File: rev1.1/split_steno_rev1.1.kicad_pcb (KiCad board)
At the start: 2 copper layers, 0 parts

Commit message: laid out switch footprints
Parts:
- added C1: 100, Capacitors_THT:CP_Radial_D5.0mm_P2.00mm, B.Cu at (170.2, 31.9)
- added D1: D, Keebio-Parts:Diode-dual, B.Cu at (65.5, 95.2)
- added D10: D, Keebio-Parts:Diode-dual, B.Cu at (141.7, 114.3)
- added D11: D, Keebio-Parts:Diode-dual, B.Cu at (65.5, 133.3)
- added D12: D, Keebio-Parts:Diode-dual, B.Cu at (86.9, 133.3)
- added D13: D, Keebio-Parts:Diode-dual, B.Cu at (103.6, 133.3)
- added D14: D, Keebio-Parts:Diode-dual, B.Cu at (106.0, 133.3)
- added D15: D, Keebio-Parts:Diode-dual, B.Cu at (141.7, 133.3)
- added D16: D, Keebio-Parts:Diode-dual, B.Cu at (96.4, 147.6)
- added D17: D, Keebio-Parts:Diode-dual, B.Cu at (111.9, 144.1)
- added D18: D, Keebio-Parts:Diode-dual, B.Cu at (136.9, 144.1)
- added D2: D, Keebio-Parts:Diode-dual, B.Cu at (86.9, 95.2)
- added D3: D, Keebio-Parts:Diode-dual, B.Cu at (103.6, 95.2)
- added D4: D, Keebio-Parts:Diode-dual, B.Cu at (106.0, 95.2)
- added D5: D, Keebio-Parts:Diode-dual, B.Cu at (141.7, 95.2)
- added D6: D, Keebio-Parts:Diode-dual, B.Cu at (65.5, 114.3)
- added D7: D, Keebio-Parts:Diode-dual, B.Cu at (86.9, 114.3)
- added D8: D, Keebio-Parts:Diode-dual, B.Cu at (103.6, 114.3)
- added D9: D, Keebio-Parts:Diode-dual, B.Cu at (106.0, 114.3)
- added J1: i2c, Keebio-Parts:TRRS-PJ-320A, B.Cu at (158.0, 26.9)
- added J2: serial, Pin_Headers:Pin_Header_Straight_1x04_Pitch2.54mm, B.Cu at (159.0, 45.5)
- added J3: rgb, Pin_Headers:Pin_Header_Straight_1x03_Pitch2.54mm, B.Cu at (178.6, 49.7)
- added J4: icsp, Pin_Headers:Pin_Header_Straight_2x03_Pitch2.54mm, B.Cu at (159.3, 59.8)
- added J5: raw, Pin_Headers:Pin_Header_Straight_1x02_Pitch2.54mm, B.Cu at (177.0, 62.1)
- added J6: extra, Pin_Headers:Pin_Header_Straight_1x01_Pitch2.54mm, B.Cu at (168.7, 60.4)
- added MX1: MX-1U, Keebio-Parts:Hybrid_PCB_100H_Dual_hole-LED, F.Cu at (57.1, 95.2)
- added MX10: MX-1U, Keebio-Parts:Hybrid_PCB_100H_Dual_hole-LED, F.Cu at (133.3, 114.3)
- added MX11: MX-1U, Keebio-Parts:Hybrid_PCB_100H_Dual_hole-LED, F.Cu at (57.1, 133.3)
- added MX12: MX-1U, Keebio-Parts:Hybrid_PCB_100H_Dual_hole-LED, F.Cu at (76.2, 133.3)
- added MX13: MX-1U, Keebio-Parts:Hybrid_PCB_100H_Dual_hole-LED, F.Cu at (95.2, 133.3)
- added MX14: MX-1U, Keebio-Parts:Hybrid_PCB_100H_Dual_hole-LED, F.Cu at (114.3, 133.3)
- added MX15: MX-1U, Keebio-Parts:Hybrid_PCB_100H_Dual_hole-LED, F.Cu at (133.3, 133.3)
- added MX16: MX-1U, Keebio-Parts:Hybrid_PCB_100H_Dual_hole-LED, F.Cu at (104.8, 152.4)
- added MX17: MX-1U, Keebio-Parts:Hybrid_PCB_200H-dual-LED, F.Cu at (114.3, 152.4)
- added MX18: MX-1U, Keebio-Parts:Hybrid_PCB_100H_Dual_hole-LED, F.Cu at (123.8, 152.4)
- added MX19: MX-1U, Keebio-Parts:Hybrid_PCB_200H-dual-LED, F.Cu at (133.3, 152.4)
- added MX2: MX-1U, Keebio-Parts:Hybrid_PCB_100H_Dual_hole-LED, F.Cu at (76.2, 95.2)
- added MX20: MX-1U, Keebio-Parts:Hybrid_PCB_100H_Dual_hole-LED, F.Cu at (142.9, 152.4)
- added MX3: MX-1U, Keebio-Parts:Hybrid_PCB_100H_Dual_hole-LED, F.Cu at (95.2, 95.2)
- added MX4: MX-1U, Keebio-Parts:Hybrid_PCB_100H_Dual_hole-LED, F.Cu at (114.3, 95.2)
- added MX5: MX-1U, Keebio-Parts:Hybrid_PCB_100H_Dual_hole-LED, F.Cu at (133.3, 95.2)
- added MX6: MX-1U, Keebio-Parts:Hybrid_PCB_100H_Dual_hole-LED, F.Cu at (57.1, 114.3)
- added MX7: MX-1U, Keebio-Parts:Hybrid_PCB_100H_Dual_hole-LED, F.Cu at (76.2, 114.3)
- added MX8: MX-1U, Keebio-Parts:Hybrid_PCB_100H_Dual_hole-LED, F.Cu at (95.2, 114.3)
- added MX9: MX-1U, Keebio-Parts:Hybrid_PCB_100H_Dual_hole-LED, F.Cu at (114.3, 114.3)
- added Q1: BC547, TO_SOT_Packages_THT:TO-92_Inline_Narrow_Oval, B.Cu at (172.4, 41.7)
- added R1: 51, Keebio-Parts:Resistor-Hybrid, B.Cu at (109.3, 31.6)
- added R10: 51, Keebio-Parts:Resistor-Hybrid, B.Cu at (44.7, 49.1)
- added R11: 51, Keebio-Parts:Resistor-Hybrid, B.Cu at (44.7, 44.0)
- added R12: 51, Keebio-Parts:Resistor-Hybrid, B.Cu at (74.7, 41.4)
- added R13: 51, Keebio-Parts:Resistor-Hybrid, B.Cu at (64.9, 31.1)
- added R14: 51, Keebio-Parts:Resistor-Hybrid, B.Cu at (99.5, 36.7)
- added R15: 51, Keebio-Parts:Resistor-Hybrid, B.Cu at (54.5, 59.5)
- added R16: 51, Keebio-Parts:Resistor-Hybrid, B.Cu at (84.5, 41.4)
- added R17: 51, Keebio-Parts:Resistor-Hybrid, B.Cu at (64.9, 36.3)
- added R18: 51, Keebio-Parts:Resistor-Hybrid, B.Cu at (74.7, 46.5)
- added R19: 470, Keebio-Parts:Resistor-Hybrid, B.Cu at (84.5, 51.6)
- added R2: 51, Keebio-Parts:Resistor-Hybrid, B.Cu at (54.5, 44.0)
- added R20: 1k, Keebio-Parts:Resistor-Hybrid, B.Cu at (64.9, 26.0)
- added R21: 4.7k, Keebio-Parts:Resistor-Hybrid, B.Cu at (119.1, 31.6)
- added R22: 4.7k, Keebio-Parts:Resistor-Hybrid, B.Cu at (74.7, 31.1)
- added R3: 51, Keebio-Parts:Resistor-Hybrid, B.Cu at (84.5, 36.2)
- added R4: 51, Keebio-Parts:Resistor-Hybrid, B.Cu at (84.5, 31.0)
- added R5: 51, Keebio-Parts:Resistor-Hybrid, B.Cu at (74.7, 26.0)
- added R6: 51, Keebio-Parts:Resistor-Hybrid, B.Cu at (119.1, 36.8)
- added R7: 51, Keebio-Parts:Resistor-Hybrid, B.Cu at (128.9, 36.8)
- added R8: 51, Keebio-Parts:Resistor-Hybrid, B.Cu at (54.5, 49.1)
- added R9: 51, Keebio-Parts:Resistor-Hybrid, B.Cu at (54.5, 54.3)
- added SW1: reset, Keebio-Parts:SW_Tactile_SPST_Angled_MJTP1117, B.Cu at (174.1, 50.5)
- added U1: ProMicro, Keebio-Parts:ArduinoProMicro, B.Cu at (76.2, 95.2)

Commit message: laid out led matrix
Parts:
- added REF**: i2c, Keebio-Parts:TRRS-PJ-320A, F.Cu at (125.0, 78.0)
- added REF**: , Mounting_Holes:MountingHole_3.2mm_M3_Pad, F.Cu at (55.1, 83.6)
- added REF**: , Mounting_Holes:MountingHole_3.2mm_M3_Pad, F.Cu at (137.5, 84.2)
- added REF**: , Mounting_Holes:MountingHole_3.2mm_M3_Pad, F.Cu at (146.4, 138.4)
- added REF**: , Mounting_Holes:MountingHole_3.2mm_M3_Pad, F.Cu at (66.7, 142.3)
- moved R17 133.0 mm to (111.9, 160.7)
- moved Q1 132.9 mm to (67.9, 123.8)
- moved R18 129.5 mm to (135.7, 160.7)
- moved R15 115.5 mm to (135.7, 141.7)
- moved R10 115.1 mm to (133.3, 122.6)
- moved R13 114.6 mm to (95.2, 141.7)
- moved J6 113.8 mm to (65.5, 108.3)
- moved R16 106.7 mm to (94.1, 147.6), turned to 270 degrees
- moved R6 105.9 mm to (57.1, 122.6)
- moved R14 105.7 mm to (111.9, 141.7)
- moved R7 100.8 mm to (76.2, 122.6)
- moved R12 100.3 mm to (76.2, 141.7)
- moved J4 98.9 mm to (62.8, 81.3)
- moved R11 98.5 mm to (57.1, 141.7)
- moved R5 97.3 mm to (133.3, 103.6)
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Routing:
- net VCC: track 0.00 -> 4.24 mm
- net /d1: track 0.00 -> 1.54 mm
- net /d2: track 0.00 -> 1.40 mm

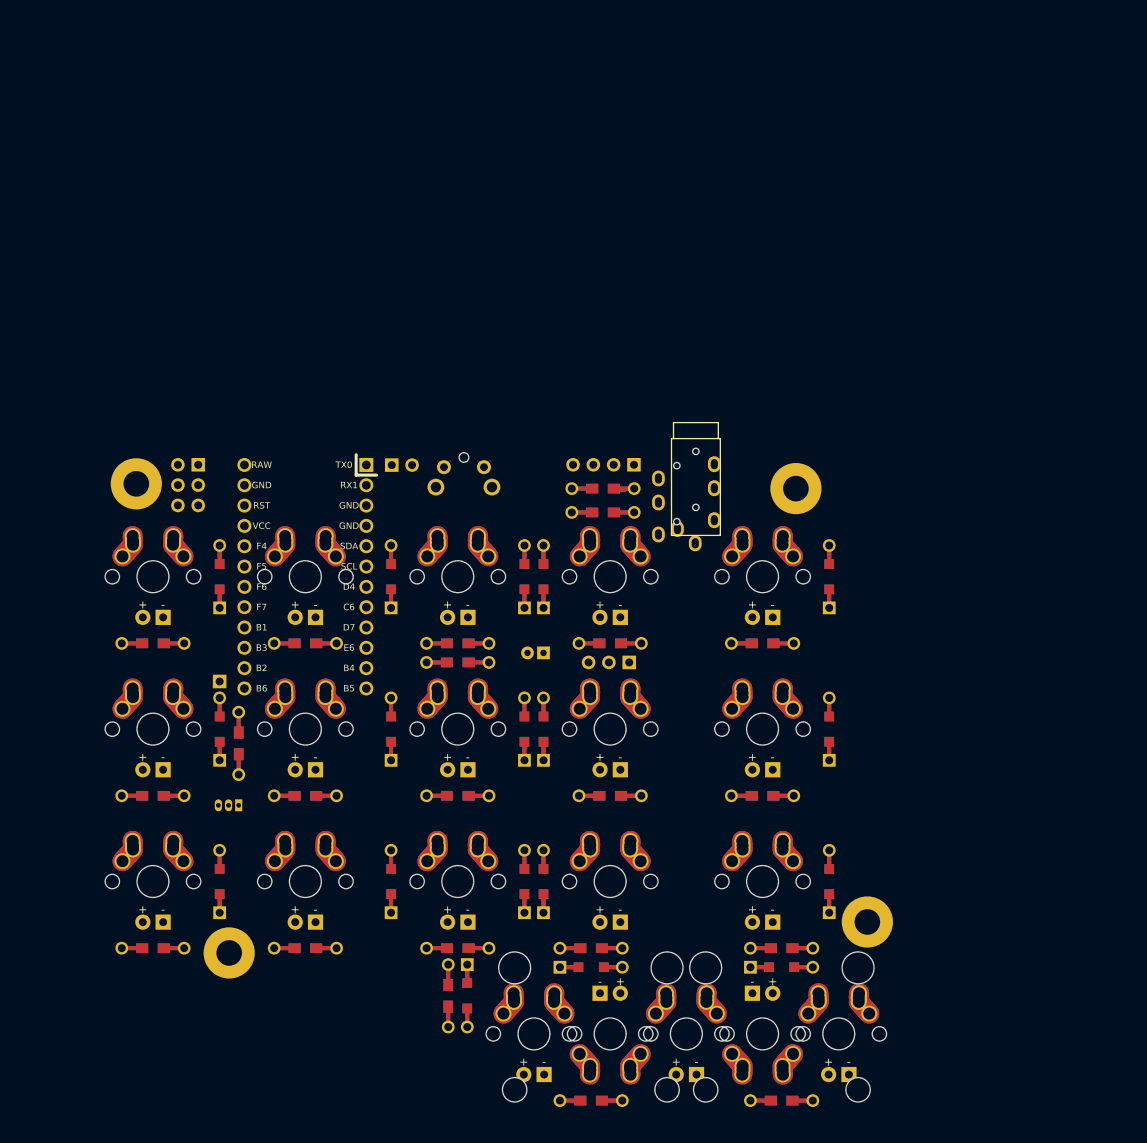
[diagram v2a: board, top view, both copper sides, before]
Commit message: laid out mounting holes
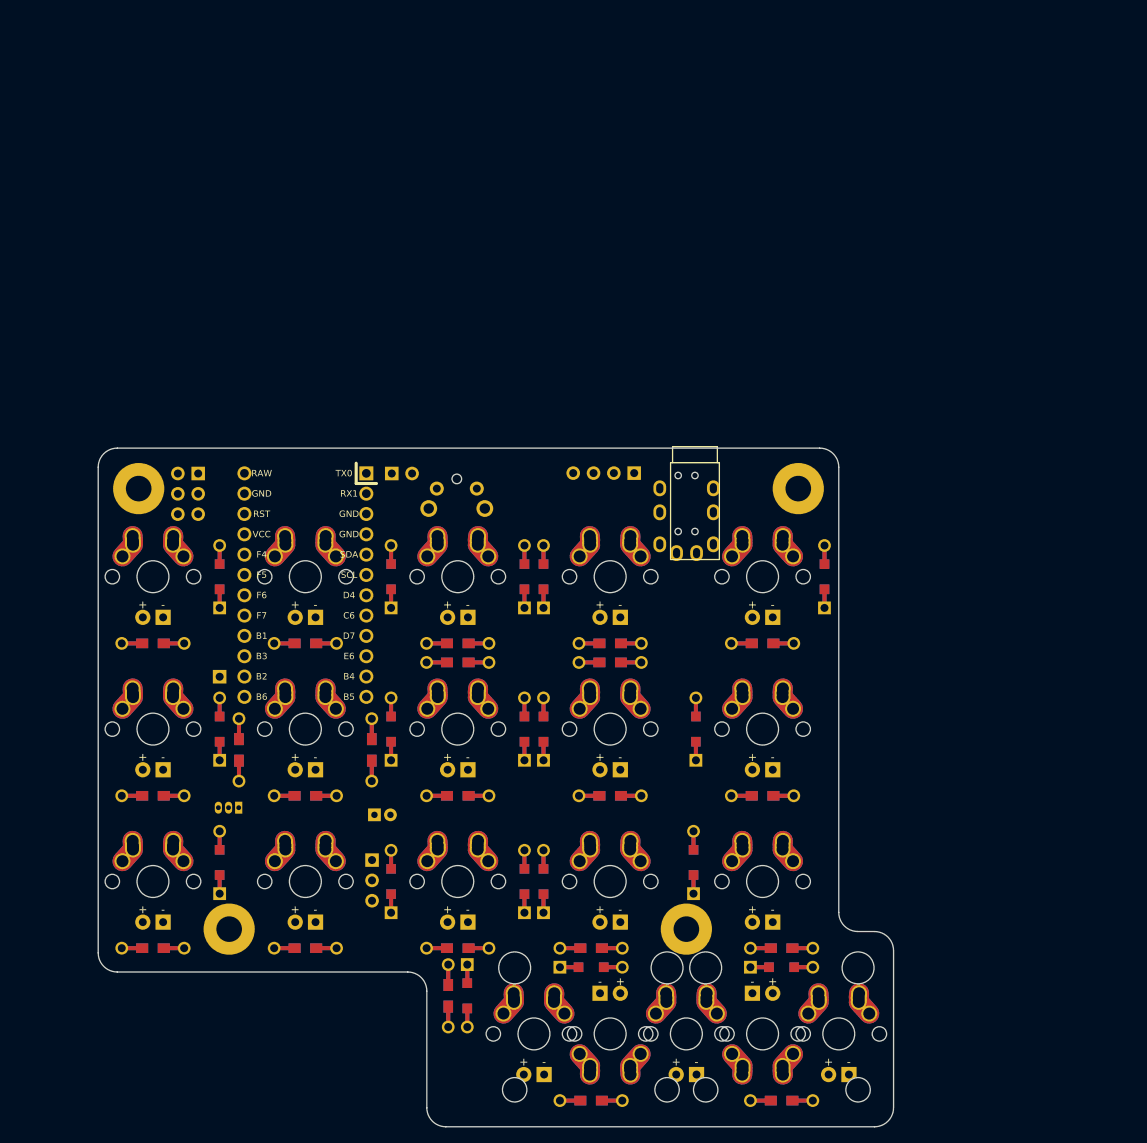
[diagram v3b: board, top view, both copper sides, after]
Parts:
- added G***: LOGO, airi_logo:airi_icon-7.6, B.Cu at (96.1, 158.9)
- added G***: LOGO, airi_logo:airi_icon-7.6, F.Cu at (96.1, 158.9)
- moved J3 40.5 mm to (84.5, 130.7), turned to 180 degrees
- moved C1 29.3 mm to (84.8, 125.0), turned to 0 degrees
- moved R21 26.1 mm to (95.3, 106.0)
- moved REF** 22.6 mm to (123.8, 139.3)
- moved R22 21.7 mm to (114.3, 106.0)
- moved D15 17.1 mm to (124.7, 131.0)
- moved D10 16.7 mm to (125.0, 114.3)
- moved R19 15.3 mm to (84.5, 116.9), turned to 270 degrees
- moved REF** 3.02 mm to (124.9, 81.0)
- moved REF** 2.98 mm to (66.7, 139.3)
- moved SW1 2.82 mm to (97.6, 84.2)
- moved D11 2.38 mm to (65.5, 131.0)
- moved J1 1.24 mm to (122.8, 81.0)
- moved J4 1.09 mm to (62.8, 82.3)
- moved J5 1.05 mm to (87.0, 82.3)
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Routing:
- net VCC: track 4.24 -> 0.00 mm
- net /d1: track 1.54 -> 0.00 mm
- net /d2: track 1.40 -> 0.00 mm
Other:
- board outline added: 99.4 x 84.8 mm

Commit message: routed non-switch traces
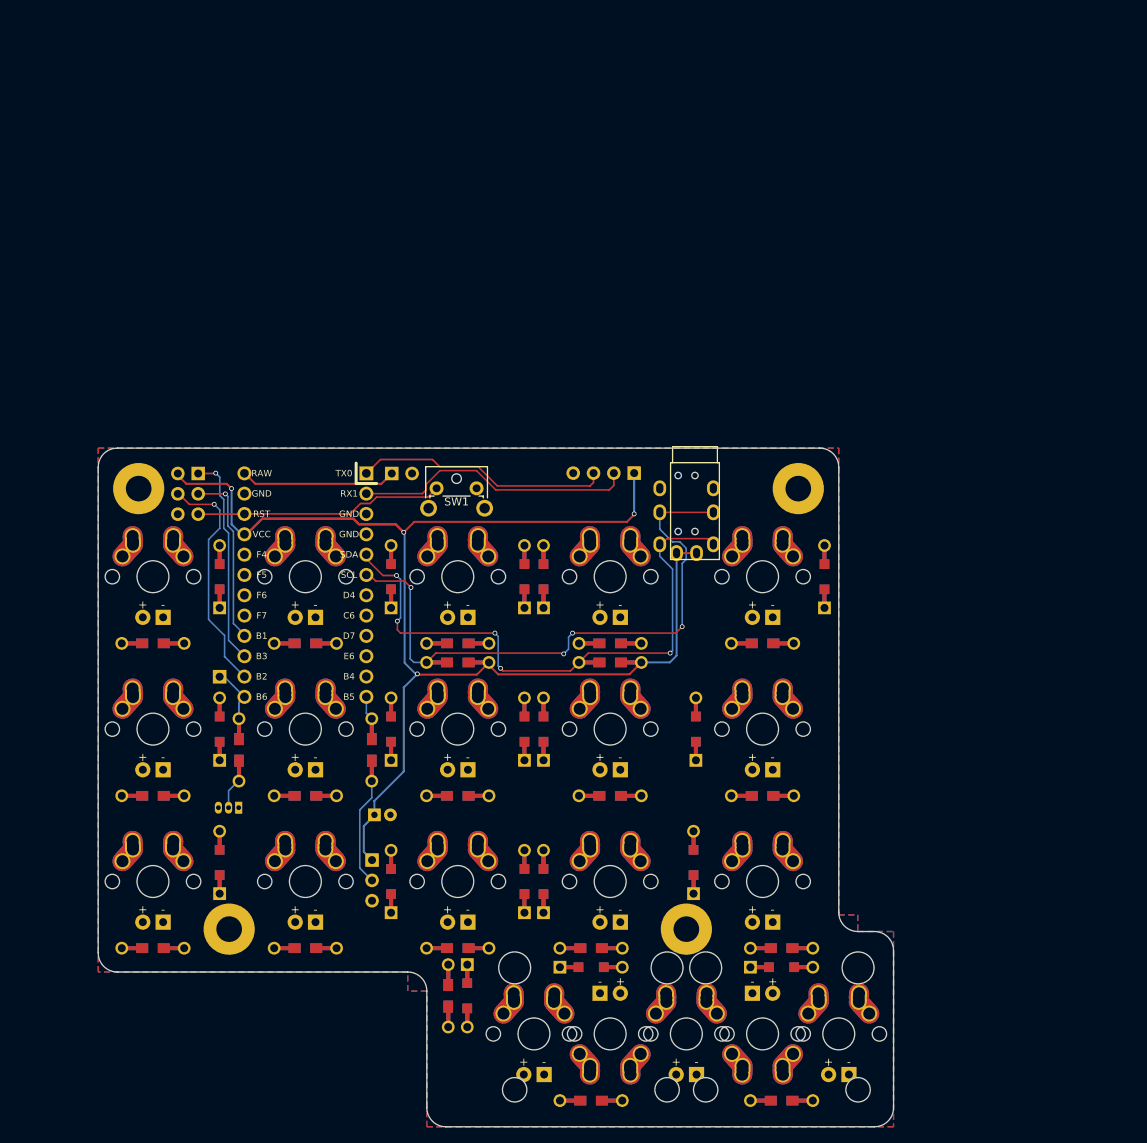
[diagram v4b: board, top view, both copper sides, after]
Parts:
- SW1: moved to F.Cu
- moved R21 19.1 mm to (114.3, 106.0)
- moved R22 19.1 mm to (95.3, 106.0)
- moved SW1 5.03 mm to (92.6, 84.2), turned to 0 degrees
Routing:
- net VCC: track 0.00 -> 191.7 mm, vias 0 -> 4
- net /d1: track 0.00 -> 77.5 mm, vias 0 -> 5
- net /d2: track 0.00 -> 76.7 mm, vias 0 -> 4
- net /rx: track 0.00 -> 35.3 mm
- net /tx: track 0.00 -> 31.8 mm
- net /rst: track 0.00 -> 31.2 mm
- net /mosi: track 0.00 -> 29.3 mm, vias 0 -> 1
- net /miso: track 0.00 -> 26.6 mm, vias 0 -> 1
- net /sclk: track 0.00 -> 22.1 mm, vias 0 -> 1
- net +6V: track 0.00 -> 19.5 mm
- net Net-(J3-Pad2): track 0.00 -> 13.7 mm
- net /d4: track 0.00 -> 7.15 mm
- net Net-(Q1-Pad2): track 0.00 -> 3.92 mm
- net /d3: track 0.00 -> 3.01 mm
- added copper zone on B.Cu, net GND
- added copper zone on F.Cu, net GND

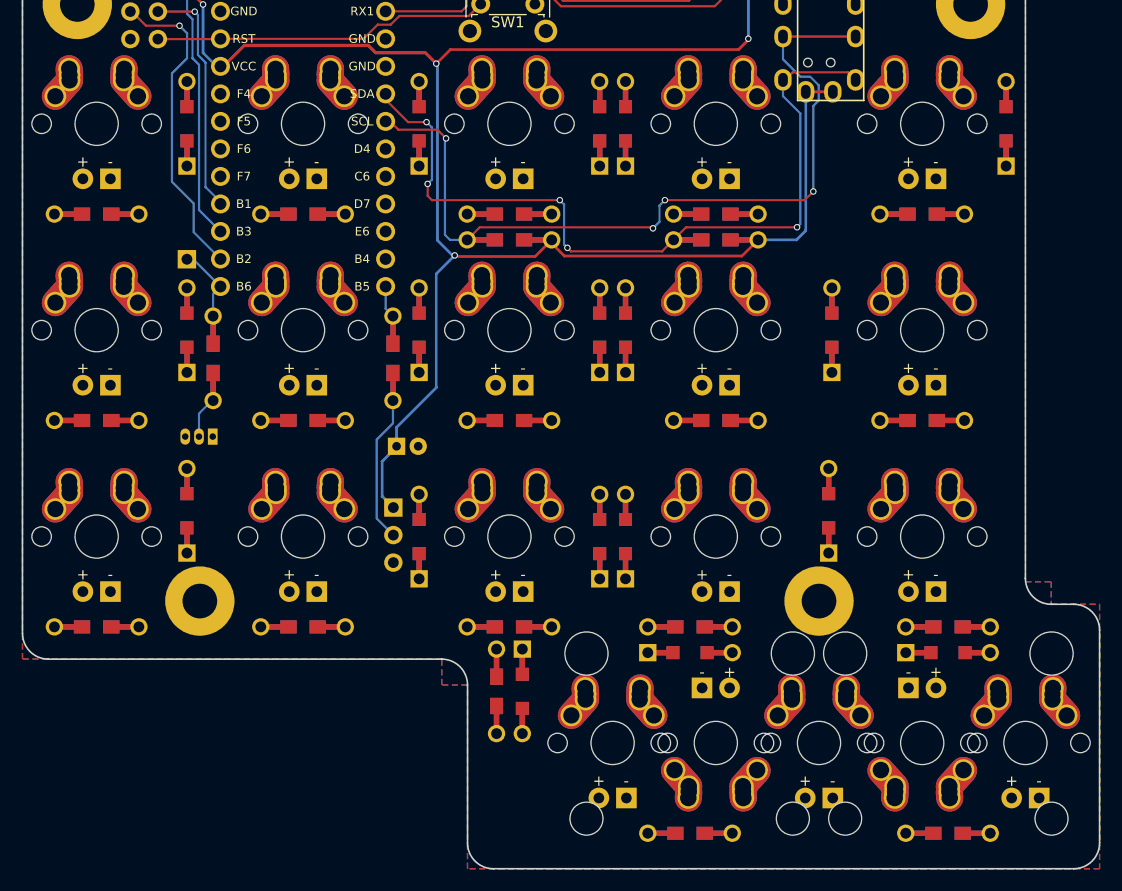
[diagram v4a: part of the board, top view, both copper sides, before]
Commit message: led/switch routing unfinished - pausing here
will pause for now - will focus on clean routing and breakouts without leds
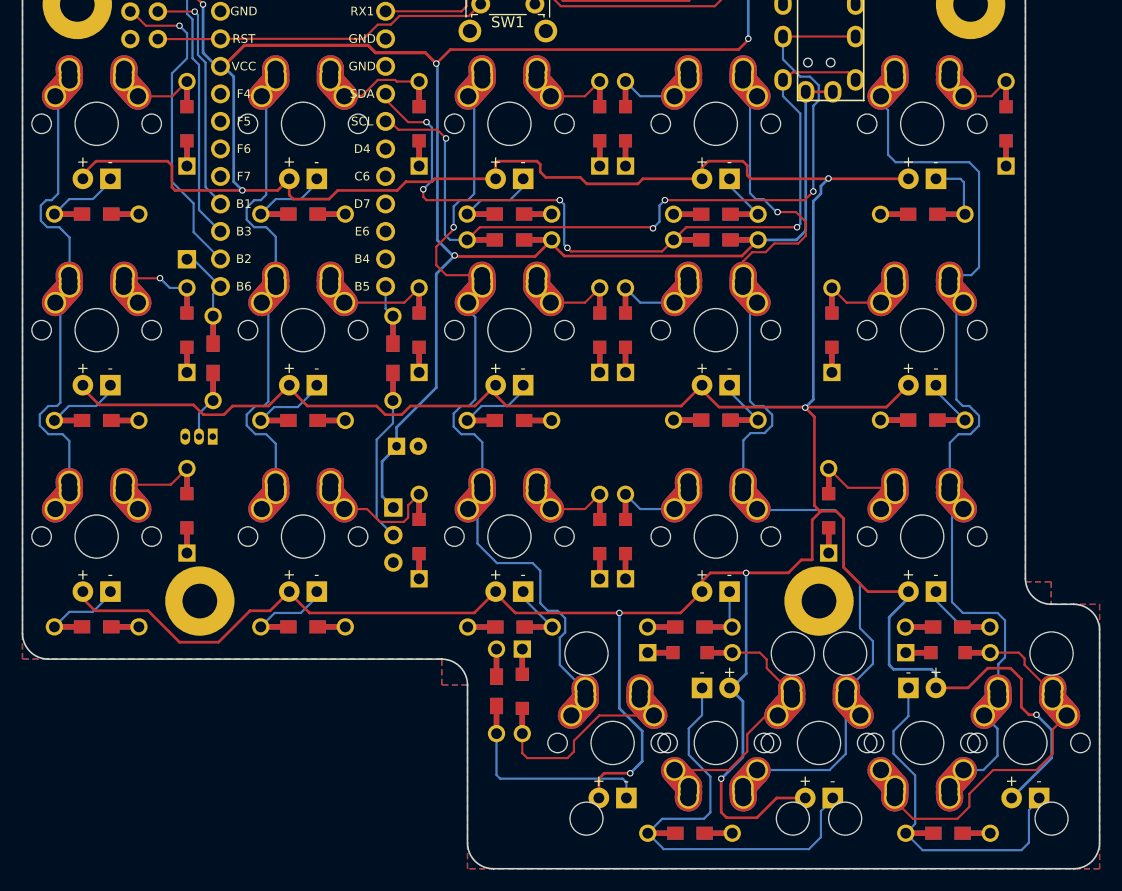
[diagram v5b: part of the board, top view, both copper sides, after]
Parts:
- moved R10 0.06 mm to (133.4, 122.6), turned to 0 degrees
- moved R5 0.05 mm to (133.4, 103.6), turned to 0 degrees
- moved R13 0.05 mm to (95.3, 141.7), turned to 0 degrees
- turned R15 to 0 degrees
- turned R9 to 0 degrees
- turned R14 to 0 degrees
- turned R4 to 0 degrees
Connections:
- MX10 pad 1: /c5 -> Net-(D10-Pad2)
- MX10 pad 2: Net-(D10-Pad2) -> /c5
- MX14 pad 1: /c4 -> Net-(D14-Pad2)
- MX14 pad 2: Net-(D14-Pad2) -> /c4
- MX15 pad 1: /c5 -> Net-(D15-Pad2)
- MX15 pad 2: Net-(D15-Pad2) -> /c5
- MX18 pad 1: /c4 -> Net-(D17-Pad2)
- MX18 pad 2: Net-(D17-Pad2) -> /c4
- MX4 pad 1: /c4 -> Net-(D4-Pad2)
- MX4 pad 2: Net-(D4-Pad2) -> /c4
- MX9 pad 1: /c4 -> Net-(D9-Pad2)
- MX9 pad 2: Net-(D9-Pad2) -> /c4
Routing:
- net VCC: track 191.7 -> 595.1 mm, vias 4 -> 12
- net /c4: track 0.00 -> 87.6 mm, vias 0 -> 1
- net /c5: track 0.00 -> 78.5 mm
- net /c3: track 0.00 -> 68.7 mm, vias 0 -> 1
- net /c1: track 0.00 -> 43.0 mm
- net /c2: track 0.00 -> 41.4 mm
- net Net-(MX17-Pad4): track 0.00 -> 40.5 mm
- net Net-(MX19-Pad4): track 0.00 -> 32.0 mm
- net Net-(D18-Pad2): track 0.00 -> 31.8 mm
- net Net-(D17-Pad2): track 0.00 -> 21.9 mm
- net Net-(D16-Pad2): track 0.00 -> 18.8 mm
- net Net-(MX16-Pad4): track 0.00 -> 17.5 mm
- net Net-(D12-Pad2): track 0.00 -> 10.3 mm
- net Net-(D2-Pad2): track 0.00 -> 8.79 mm
- net Net-(D7-Pad2): track 0.00 -> 8.67 mm
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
